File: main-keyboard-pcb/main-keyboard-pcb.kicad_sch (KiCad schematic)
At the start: 159 parts, among them IC1 LMR51420XDDCR, SW1 SW_SPDT, SW10 SW_Push, SW11 SW_Push, SW12 SW_Push, SW13 SW_Push, SW14 SW_Push, SW15 SW_Push, SW16 SW_Push, SW17 SW_Push, SW18 SW_Push, SW19 SW_Push, SW2 SW_Push, SW20 SW_Push, SW21 SW_Push, SW22 SW_Push, SW23 SW_Push, SW24 SW_Push, SW25 SW_Push, SW26 SW_Push, SW27 SW_Push, SW28 SW_Push, SW29 SW_Push, SW3 SW_Push, SW30 SW_Push, SW31 SW_Push, SW32 SW_Push, SW33 SW_Push, SW34 SW_Push, SW35 SW_Push, SW36 SW_Push, SW37 SW_Push, SW38 SW_Push, SW39 SW_Push, SW4 SW_Push, SW40 SW_Push, SW41 SW_Push, SW42 SW_Push, SW43 SW_Push, SW44 SW_Push, SW45 SW_Push, SW46 SW_Push, SW47 SW_Push, SW48 SW_Push, SW49 SW_Push, SW5 SW_Push, SW50 SW_Push, SW51 SW_Push, SW52 SW_Push, SW53 SW_Push, SW54 SW_Push, SW55 SW_Push, SW56 SW_Push, SW57 SW_Push, SW58 SW_Push, SW59 SW_Push, SW6 SW_Push, SW60 SW_Push, SW61 SW_Push, SW62 SW_Push, SW63 SW_Push, SW64 SW_Push, SW65 SW_Push, SW66 SW_Push, SW67 SW_Push, SW68 SW_Push, SW7 SW_Push, SW8 SW_Push, SW9 SW_Push, U2 STM32F407VGT6, Y1 16MHz

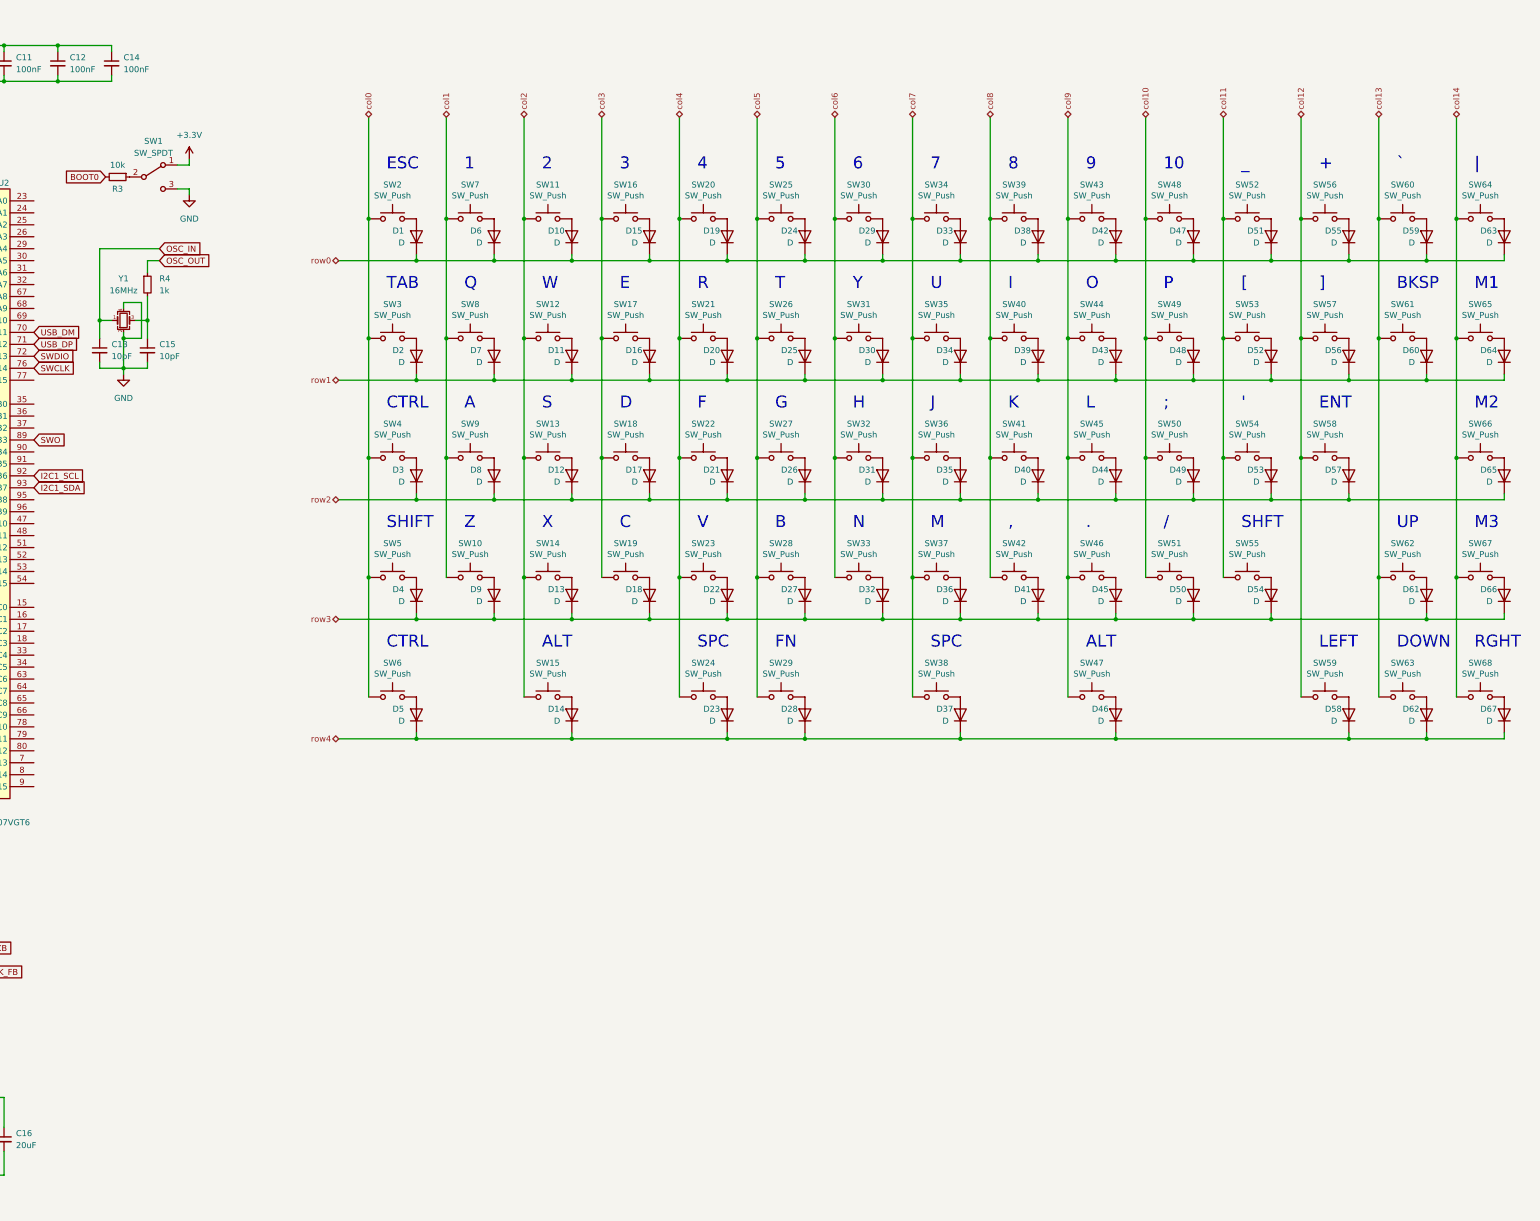
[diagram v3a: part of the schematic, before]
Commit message: Removed old traces and routing
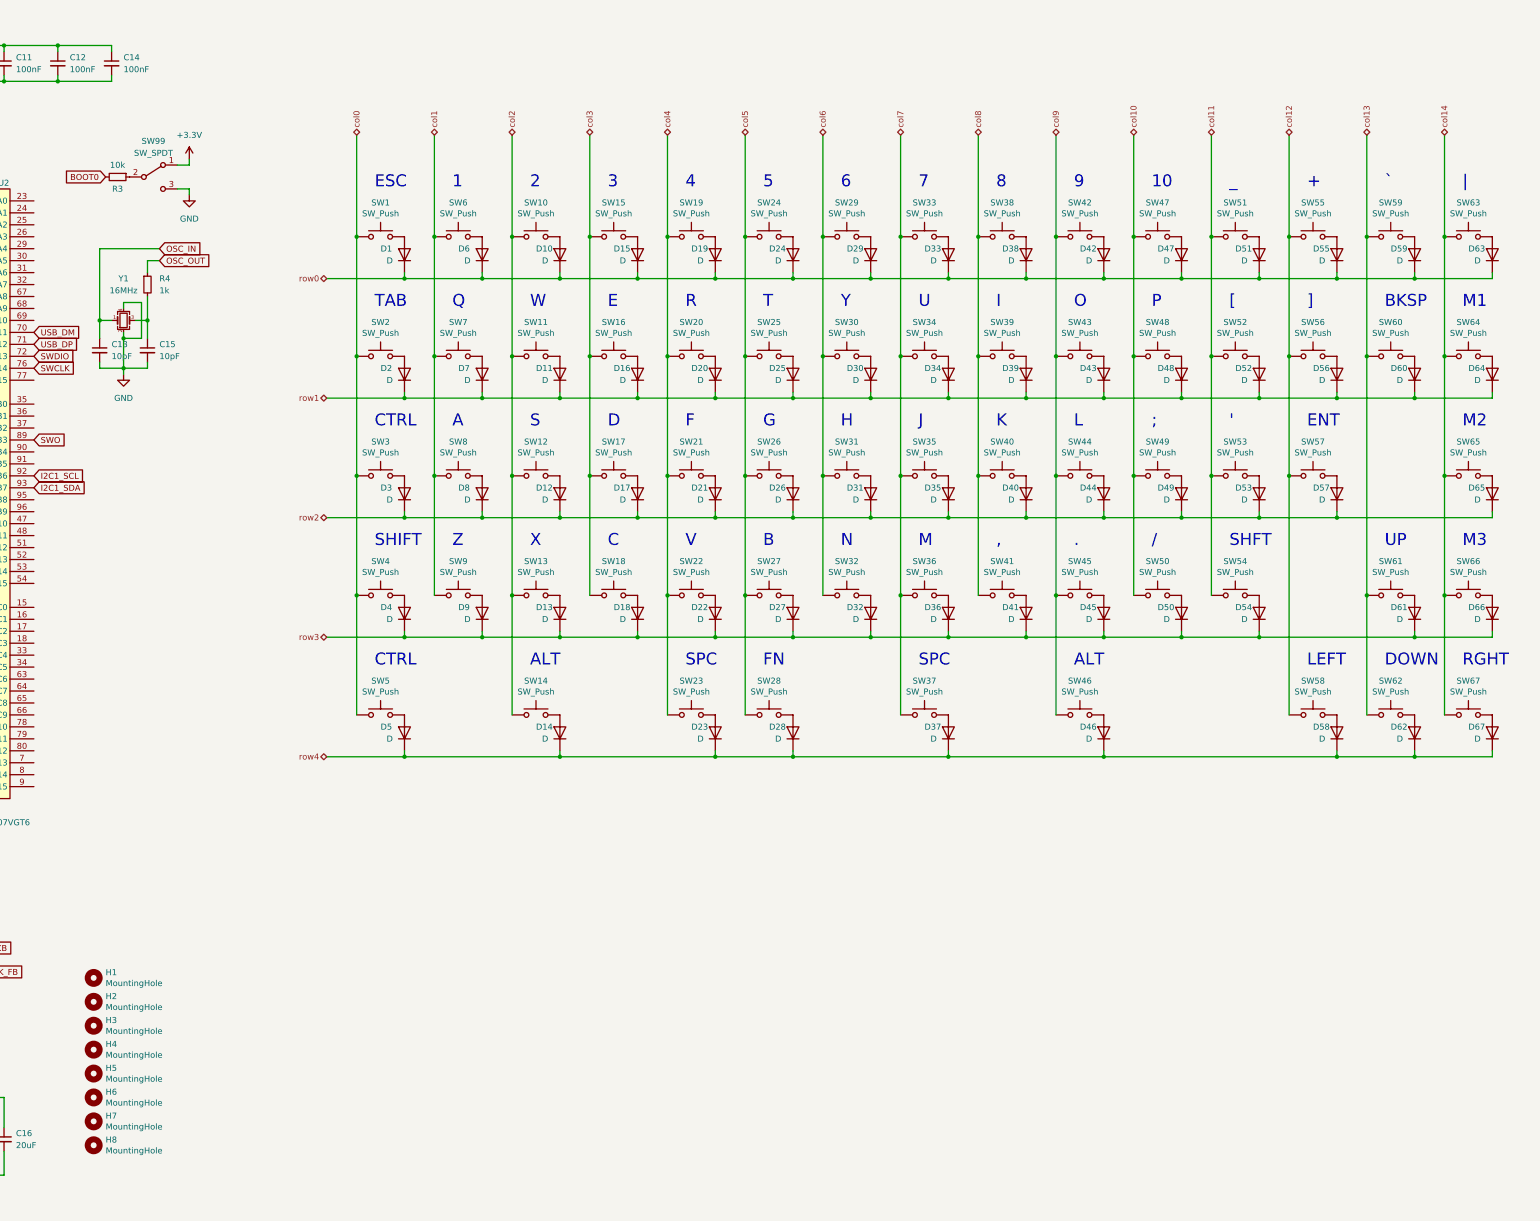
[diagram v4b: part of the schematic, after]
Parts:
- removed SW68: SW_Push, MX_Switch:SW_Cherry_MX_1.00u_PCB, symbol Switch:SW_Push
- added H1, H2, H3, H4, H5, H6, H7, H8: MountingHole, Mounting_Holes:MountingHole_2.2mm_M2_Pad, symbol Mechanical:MountingHole
- added SW1: SW_Push, MX_Switch:SW_Cherry_MX_1.00u_PCB, symbol Switch:SW_Push
- SW14, SW2, SW46, SW60: footprint MX_Switch:SW_Cherry_MX_1.00u_PCB -> MX_Switch:SW_Cherry_MX_1.50u_PCB
- SW15, SW47, SW6, SW61: footprint MX_Switch:SW_Cherry_MX_1.50u_PCB -> MX_Switch:SW_Cherry_MX_1.00u_PCB
- SW23: footprint MX_Switch:SW_Cherry_MX_1.00u_PCB -> MX_Switch:SW_Cherry_MX_2.00u_PCB_ReversedStabilizers
- SW24: footprint MX_Switch:SW_Cherry_MX_2.00u_PCB_ReversedStabilizers -> MX_Switch:SW_Cherry_MX_1.00u_PCB
- SW3: footprint MX_Switch:SW_Cherry_MX_1.50u_PCB -> MX_Switch:SW_Cherry_MX_1.75u_PCB
- SW37: footprint MX_Switch:SW_Cherry_MX_1.00u_PCB -> MX_Switch:SW_Cherry_MX_2.75u_PCB_ReversedStabilizers
- SW38: footprint MX_Switch:SW_Cherry_MX_2.75u_PCB_ReversedStabilizers -> MX_Switch:SW_Cherry_MX_1.00u_PCB
- SW4: footprint MX_Switch:SW_Cherry_MX_1.75u_PCB -> MX_Switch:SW_Cherry_MX_2.25u_PCB
- SW5: footprint MX_Switch:SW_Cherry_MX_2.25u_PCB -> MX_Switch:SW_Cherry_MX_1.50u_PCB
- SW54: footprint MX_Switch:SW_Cherry_MX_1.00u_PCB -> MX_Switch:SW_Cherry_MX_1.75u_PCB
- SW55: footprint MX_Switch:SW_Cherry_MX_1.75u_PCB -> MX_Switch:SW_Cherry_MX_1.00u_PCB
- SW57: footprint MX_Switch:SW_Cherry_MX_1.00u_PCB -> MX_Switch:SW_Cherry_MX_2.25u_PCB_ReversedStabilizers
- SW58: footprint MX_Switch:SW_Cherry_MX_2.25u_PCB_ReversedStabilizers -> MX_Switch:SW_Cherry_MX_1.00u_PCB
- renumbered SW1 to SW99
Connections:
- net col0: now also SW1.1; no longer SW6.1
- net col1: now also SW6.1; no longer SW10.1
- net col10: now also SW47.1; no longer SW51.1
- net col11: now also SW51.1; no longer SW55.1
- net col12: now also SW55.1; no longer SW59.1
- net col13: now also SW59.1; no longer SW63.1
- net col14: now also SW63.1
- net col2: now also SW10.1; no longer SW15.1
- net col3: now also SW15.1; no longer SW19.1
- net col4: now also SW19.1; no longer SW24.1
- net col5: now also SW24.1; no longer SW29.1
- net col6: now also SW29.1; no longer SW33.1
- net col7: now also SW33.1; no longer SW38.1
- net col8: now also SW38.1; no longer SW42.1
- net col9: now also SW42.1; no longer SW47.1
- net at SW20.2: now also D20.2 (A); no longer D19.2 (A)
- net at D7.2 (A): now also SW7.2; no longer SW8.2
- net at D23.2 (A): now also SW23.2; no longer SW24.2
- net at SW30.2: now also D30.2 (A); no longer D29.2 (A)
- net at SW56.2: now also D56.2 (A); no longer D55.2 (A)
- net at D32.2 (A): now also SW32.2; no longer SW33.2
- net at SW6.2: now also D6.2 (A); no longer D5.2 (A)
- net at SW58.2: now also D58.2 (A); no longer D57.2 (A)
- net at SW10.2: now also D10.2 (A); no longer D9.2 (A)
- net at D54.2 (A): now also SW54.2; no longer SW55.2
- net at D14.2 (A): now also SW14.2; no longer SW15.2
- net at SW59.2: now also D59.2 (A); no longer D58.2 (A)
- net at D13.2 (A): now also SW13.2; no longer SW14.2
- net at D67.2 (A): now also SW67.2
- net at SW61.2: now also D61.2 (A); no longer D60.2 (A)
- net at SW35.2: now also D35.2 (A); no longer D34.2 (A)
- net at D17.2 (A): now also SW17.2; no longer SW18.2
- net at SW50.2: now also D50.2 (A); no longer D49.2 (A)
- net at D46.2 (A): now also SW46.2; no longer SW47.2
- net at SW36.2: now also D36.2 (A); no longer D35.2 (A)
- net at SW16.2: now also D16.2 (A); no longer D15.2 (A)
- net at D48.2 (A): now also SW48.2; no longer SW49.2
- net at D53.2 (A): now also SW53.2; no longer SW54.2
- net at D25.2 (A): now also SW25.2; no longer SW26.2
- net at SW52.2: now also D52.2 (A); no longer D51.2 (A)
- net at D11.2 (A): now also SW11.2; no longer SW12.2
- net at D44.2 (A): now also SW44.2; no longer SW45.2
- net at SW66.2: now also D66.2 (A); no longer D65.2 (A)
- net at SW40.2: now also D40.2 (A); no longer D39.2 (A)
- net at D63.2 (A): now also SW63.2; no longer SW64.2
- net at SW41.2: now also D41.2 (A); no longer D40.2 (A)
- net at SW42.2: now also D42.2 (A); no longer D41.2 (A)
- net at D2.2 (A): now also SW2.2; no longer SW3.2
- net at D18.2 (A): now also SW18.2; no longer SW19.2
- net at SW62.2: now also D62.2 (A); no longer D61.2 (A)
- net at SW57.2: now also D57.2 (A); no longer D56.2 (A)
- net at SW4.2: now also D4.2 (A); no longer D3.2 (A)
- net at D37.2 (A): now also SW37.2; no longer SW38.2
- net at SW65.2: now also D65.2 (A); no longer D64.2 (A)
- net at SW9.2: now also D9.2 (A); no longer D8.2 (A)
- net at D43.2 (A): now also SW43.2; no longer SW44.2
- net at SW5.2: now also D5.2 (A); no longer D4.2 (A)
- net at D45.2 (A): now also SW45.2; no longer SW46.2
- net at D28.2 (A): now also SW28.2; no longer SW29.2
- net at SW51.2: now also D51.2 (A); no longer D50.2 (A)
- net at SW31.2: now also D31.2 (A); no longer D30.2 (A)
- net at SW34.2: now also D34.2 (A); no longer D33.2 (A)
- net at D21.2 (A): now also SW21.2; no longer SW22.2
- net at D24.2 (A): now also SW24.2; no longer SW25.2
- net at D27.2 (A): now also SW27.2; no longer SW28.2
- net at D12.2 (A): now also SW12.2; no longer SW13.2
- net at D22.2 (A): now also SW22.2; no longer SW23.2
- net at D26.2 (A): now also SW26.2; no longer SW27.2
- net at SW39.2: now also D39.2 (A); no longer D38.2 (A)
- net at D1.2 (A): now also SW1.2; no longer SW2.2
- net at SW60.2: now also D60.2 (A); no longer D59.2 (A)
- net at D47.2 (A): now also SW47.2; no longer SW48.2
- new net: D29.2 (A), SW29.2
- new net: D38.2 (A), SW38.2
- new net: D3.2 (A), SW3.2
- new net: D15.2 (A), SW15.2
- new net: D33.2 (A), SW33.2
- new net: D8.2 (A), SW8.2
- new net: D55.2 (A), SW55.2
- new net: D64.2 (A), SW64.2
- new net: D19.2 (A), SW19.2
- new net: D49.2 (A), SW49.2

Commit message: Updated diodes
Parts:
- D1, D10, D11, D12, D13, D14, D15, D16, D17, D18, D19, D2, D20, D21, D22, D23, D24, D25, D26, D27, D28, D29, D3, D30, D31, D32, D33, D34, D35, D36, D37, D38, D39, D4, D40, D41, D42, D43, D44, D45, D46, D47, D48, D49, D5, D50, D51, D52, D53, D54, D55, D56, D57, D58, D59, D6, D60, D61, D62, D63, D64, D65, D66, D67, D7, D8, D9: footprint Diodes_SMD:D_SOD-123 -> DIODES_KEEB_2:1N4148W-13-F

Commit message: Completed footprint library for main-keyboard and rough part placement
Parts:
- added C17: 0.1uF, stm32f4_2:GRM022R61A104ME01L, symbol Device:C_Small
- added J1: Debug SWD Connector, Connector_PinHeader_1.27mm:PinHeader_2x05_P1.27mm_Vertical_SMD, symbol Connector_Generic:Conn_02x05_Odd_Even
- added J2: Hotplug, Connector_PinHeader_2.54mm:PinHeader_1x04_P2.54mm_Vertical, symbol Connector_Generic:Conn_01x04
- added J3: USB_B_Micro, stm32f4_2:USB307530A, symbol Connector:USB_B_Micro
- added R5, R6: 2.2k, stm32f4_2:ERJ-UP3F2201V, symbol Device:R_Small
- added U1: USBLC6-4SC6, Package_TO_SOT_SMD:SOT-23-6, symbol Power_Protection:USBLC6-4SC6
- C1, C4: footprint (none) -> stm32f4_2:GRM155R61E225KE11D
- C10, C11, C12, C14, C5, C6, C7: value 100nF -> 0.1uF; footprint (none) -> stm32f4_2:GRM022R61A104ME01L
- C13, C15: footprint (none) -> stm32f4_2:GRM0225C1C100FA03L
- C16, C9: footprint (none) -> buck-converter:GRMJN7R61C206ME05D
- C2, C3: footprint (none) -> stm32f4_2:GRM188R61C475KAAJD
- C8: value C_Small -> 0.1uF; footprint (none) -> stm32f4_2:GRM022R61A104ME01L
- L1: value 25uH -> 15uH; footprint (none) -> buck-converter:SRP1265WA150M
- R1: footprint (none) -> buck-converter:CHV1206AJW-104ELF
- R2: footprint (none) -> buck-converter:ERJP08F2212V
- R3: footprint (none) -> stm32f4_2:ERJ-UP3F1002V
- R4: footprint (none) -> stm32f4_2:ERJ-UP3D1001V
- SW99: footprint (none) -> Button_Switch_SMD:SW_SPDT_PCM12
- U2: footprint stm32f4_2:QFP50P1600X1600X160-100N -> Package_QFP:LQFP-100_14x14mm_P0.5mm
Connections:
- net +3.3V is gone; now on net +3V3: C10.1, C11.1, C12.1, C14.1, C2.1, C5.1, C6.1, C7.1, SW99.1 (A), U2.100 (VDD), U2.11 (VDD), U2.19 (VDD), U2.22 (VDDA), U2.28 (VDD), U2.50 (VDD), U2.6 (VBAT), U2.75 (VDD)
- net +5V: now also J3.1 (VBUS), U1.5 (VBUS)
- net GND: now also C17.2, J1.3 (Pin_3), J1.5 (Pin_5), J1.9 (Pin_9), J2.4 (Pin_4), J3.5 (GND), U1.2 (GND)
- net I2C1_SCL: now also J2.2 (Pin_2), R5.2
- net I2C1_SDA: now also J2.3 (Pin_3), R6.2
- net NRST: now also J1.10 (Pin_10)
- net SWCLK: now also J1.4 (Pin_4)
- net SWDIO: now also J1.2 (Pin_2)
- net SWO: now also J1.6 (Pin_6)
- net col0: now also U2.29 (PA4)
- net col1: now also U2.30 (PA5)
- net col10: now also U2.55 (PD8)
- net col11: now also U2.54 (PB15)
- net col12: now also U2.53 (PB14)
- net col13: now also U2.52 (PB13)
- net col14: now also U2.51 (PB12)
- net col2: now also U2.31 (PA6)
- net col3: now also U2.32 (PA7)
- net col4: now also U2.33 (PC4)
- net col5: now also U2.34 (PC5)
- net col6: now also U2.35 (PB0)
- net col7: now also U2.58 (PD11)
- net col8: now also U2.57 (PD10)
- net col9: now also U2.56 (PD9)
- net row0: now also U2.1 (PE2)
- net row1: now also U2.2 (PE3)
- net row2: now also U2.3 (PE4)
- net row3: now also U2.4 (PE5)
- net row4: now also U2.5 (PE6)
- net +3V3: now reaches C16.1, C9.1, L1.2, R1.1
- net +3V3: now also C17.1, J1.1 (Pin_1), J2.1 (Pin_1), R5.1, R6.1
- net USB_DM renamed USB_CONN_DM
- net USB_CONN_DM: now also J3.2 (D-), U1.3 (I/O2)
- net USB_DP renamed USB_CONN_DP
- net USB_CONN_DP: now also J3.3 (D+), U1.1 (I/O1)
- no-connect marks 0 -> 60
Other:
- moved on the sheet: D1, D10, D11, D12, D13, D14, D15, D16, D17, D18, D19, D2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
